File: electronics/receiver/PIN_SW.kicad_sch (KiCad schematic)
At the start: 35 parts, among them J401 Conn_Coaxial, J402 Conn_Coaxial, J403 Conn_Coaxial, J404 Conn_01x06_Male, J405 Conn_01x01_Male, J406 Conn_Coaxial, U401 AS179-92LF, U402 AS179-92LF, U403 AMS1117-5.0, U404 AS179-92LF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

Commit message: Add values
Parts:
- C401, C402, C403, C404, C410, C412: value C -> 1n0
- C405, C406, C407, C408: value C -> 100p
- C409, C411: value C -> 100n
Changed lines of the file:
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@@
       (effects (font (size 1.27 1.27)) (justify left))
     )
-    (property "Value" "C" (id 1) (at 124.46 116.8399 0)
+    (property "Value" "100p" (id 1) (at 124.46 116.8399 0)
       (effects (font (size 1.27 1.27)) (justify left))
     )
@@
       (effects (font (size 1.27 1.27)) (justify left))
     )
-    (property "Value" "C" (id 1) (at 190.5 116.8399 0)
+    (property "Value" "100p" (id 1) (at 190.5 116.8399 0)
       (effects (font (size 1.27 1.27)) (justify left))
     )
@@
     (in_bom yes) (on_board yes) (fields_autoplaced)
     (property "Reference" "C403" (id 0) (at 66.04 147.5445 90))
-    (property "Value" "C" (id 1) (at 66.04 150.3196 90))
+    (property "Value" "1n0" (id 1) (at 66.04 150.3196 90))
     (property "Footprint" "Capacitor_SMD:C_0805_2012Metric" (id 2) (at 69.85 152.7048 0)
       (effects (font (size 1.27 1.27)) hide)
@@
     (in_bom yes) (on_board yes) (fields_autoplaced)
     (property "Reference" "C412" (id 0) (at 218.44 63.9985 90))
-    (property "Value" "C" (id 1) (at 218.44 66.7736 90))
+    (property "Value" "1n0" (id 1) (at 218.44 66.7736 90))
     (property "Footprint" "Capacitor_SMD:C_0805_2012Metric" (id 2) (at 222.25 60.6552 0)
       (effects (font (size 1.27 1.27)) hide)
@@
     (in_bom yes) (on_board yes) (fields_autoplaced)
     (property "Reference" "C404" (id 0) (at 71.12 91.9385 90))
-    (property "Value" "C" (id 1) (at 71.12 94.7136 90))
+    (property "Value" "1n0" (id 1) (at 71.12 94.7136 90))
     (property "Footprint" "Capacitor_SMD:C_0805_2012Metric" (id 2) (at 67.31 88.5952 0)
       (effects (font (size 1.27 1.27)) hide)
@@
       (effects (font (size 1.27 1.27)) (justify left))
     )
-    (property "Value" "C" (id 1) (at 179.07 116.8399 0)
+    (property "Value" "100p" (id 1) (at 179.07 116.8399 0)
       (effects (font (size 1.27 1.27)) (justify left))
     )
@@
   (symbol (lib_id "Device:C") (at 50.8 78.74 270) (unit 1)
     (in_bom yes) (on_board yes) (fields_autoplaced)
-    (property "Reference" "C402" (id 0) (at 50.8 72.6145 90))
-    (property "Value" "C" (id 1) (at 50.8 75.3896 90))
+    (property "Reference" "C402" (id 0) (at 50.8 71.12 90))
+    (property "Value" "1n0" (id 1) (at 50.8 73.66 90))
     (property "Footprint" "Capacitor_SMD:C_0805_2012Metric" (id 2) (at 46.99 79.7052 0)
       (effects (font (size 1.27 1.27)) hide)
@@
       (effects (font (size 1.27 1.27)) (justify left))
     )
-    (property "Value" "C" (id 1) (at 35.941 136.3222 0)
+    (property "Value" "1n0" (id 1) (at 35.941 136.3222 0)
       (effects (font (size 1.27 1.27)) (justify left))
     )
@@
     (in_bom yes) (on_board yes) (fields_autoplaced)
     (property "Reference" "C410" (id 0) (at 207.01 72.6145 90))
-    (property "Value" "C" (id 1) (at 207.01 75.3896 90))
+    (property "Value" "1n0" (id 1) (at 207.01 75.3896 90))
     (property "Footprint" "Capacitor_SMD:C_0805_2012Metric" (id 2) (at 210.82 79.7052 0)
       (effects (font (size 1.27 1.27)) hide)
@@
       (effects (font (size 1.27 1.27)) (justify left))
     )
-    (property "Value" "C" (id 1) (at 213.36 137.1599 0)
+    (property "Value" "100n" (id 1) (at 213.36 137.1599 0)
       (effects (font (size 1.27 1.27)) (justify left))
     )
@@
       (effects (font (size 1.27 1.27)) (justify left))
     )
-    (property "Value" "C" (id 1) (at 134.62 116.8399 0)
+    (property "Value" "100p" (id 1) (at 134.62 116.8399 0)
       (effects (font (size 1.27 1.27)) (justify left))
     )
@@
       (effects (font (size 1.27 1.27)) (justify left))
     )
-    (property "Value" "C" (id 1) (at 195.58 151.1299 0)
-      (effects (font (size 1.27 1.27)) (justify left))
-    )
+    (property "Value" "100n" (id 1) (at 195.58 151.1299 0)
+      (effects (font (size 1.27 1.27)) (justify left))
+    )

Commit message: Update values
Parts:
- R401, R402, R404, R405: value R -> 68R
- R403, R406, R408, R410: value R -> NF
- R407, R409, R411: value R -> 0R
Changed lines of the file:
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@@
+    (effects (font (size 1.27 1.27)) (justify left bottom))
+  )
+  (label "Loss = 16 dB" (at 78.74 143.51 0)
     (effects (font (size 1.27 1.27)) (justify left bottom))
   )
@@
   (symbol (lib_id "Device:R") (at 226.06 146.05 0) (unit 1)
     (in_bom yes) (on_board yes) (fields_autoplaced)
-    (property "Reference" "R411" (id 0) (at 227.838 145.2153 0)
-      (effects (font (size 1.27 1.27)) (justify left))
-    )
-    (property "Value" "R" (id 1) (at 227.838 147.7522 0)
+    (property "Reference" "R411" (id 0) (at 228.6 144.7799 0)
+      (effects (font (size 1.27 1.27)) (justify left))
+    )
+    (property "Value" "0R" (id 1) (at 228.6 147.3199 0)
       (effects (font (size 1.27 1.27)) (justify left))
     )
@@
   (symbol (lib_id "Device:R") (at 220.98 129.54 0) (unit 1)
     (in_bom yes) (on_board yes) (fields_autoplaced)
-    (property "Reference" "R408" (id 0) (at 222.758 128.7053 0)
-      (effects (font (size 1.27 1.27)) (justify left))
-    )
-    (property "Value" "R" (id 1) (at 222.758 131.2422 0)
+    (property "Reference" "R408" (id 0) (at 223.52 128.2699 0)
+      (effects (font (size 1.27 1.27)) (justify left))
+    )
+    (property "Value" "NF" (id 1) (at 223.52 130.8099 0)
       (effects (font (size 1.27 1.27)) (justify left))
     )
@@
   (symbol (lib_id "Device:R") (at 226.06 129.54 0) (unit 1)
     (in_bom yes) (on_board yes) (fields_autoplaced)
-    (property "Reference" "R410" (id 0) (at 227.838 128.7053 0)
-      (effects (font (size 1.27 1.27)) (justify left))
-    )
-    (property "Value" "R" (id 1) (at 227.838 131.2422 0)
+    (property "Reference" "R410" (id 0) (at 228.6 128.2699 0)
+      (effects (font (size 1.27 1.27)) (justify left))
+    )
+    (property "Value" "NF" (id 1) (at 228.6 130.8099 0)
       (effects (font (size 1.27 1.27)) (justify left))
     )
@@
   (symbol (lib_id "Device:R") (at 214.63 129.54 0) (unit 1)
     (in_bom yes) (on_board yes) (fields_autoplaced)
-    (property "Reference" "R406" (id 0) (at 216.408 128.7053 0)
-      (effects (font (size 1.27 1.27)) (justify left))
-    )
-    (property "Value" "R" (id 1) (at 216.408 131.2422 0)
+    (property "Reference" "R406" (id 0) (at 217.17 128.2699 0)
+      (effects (font (size 1.27 1.27)) (justify left))
+    )
+    (property "Value" "NF" (id 1) (at 217.17 130.8099 0)
       (effects (font (size 1.27 1.27)) (justify left))
     )
@@
   (symbol (lib_id "Device:R") (at 74.93 158.75 0) (unit 1)
     (in_bom yes) (on_board yes) (fields_autoplaced)
-    (property "Reference" "R401" (id 0) (at 76.708 157.8415 0)
-      (effects (font (size 1.27 1.27)) (justify left))
-    )
-    (property "Value" "R" (id 1) (at 76.708 160.6166 0)
+    (property "Reference" "R401" (id 0) (at 77.47 157.4799 0)
+      (effects (font (size 1.27 1.27)) (justify left))
+    )
+    (property "Value" "68R" (id 1) (at 77.47 160.0199 0)
       (effects (font (size 1.27 1.27)) (justify left))
     )
@@
   (symbol (lib_id "Device:R") (at 90.17 153.67 270) (unit 1)
     (in_bom yes) (on_board yes) (fields_autoplaced)
-    (property "Reference" "R404" (id 0) (at 90.17 148.6875 90))
-    (property "Value" "R" (id 1) (at 90.17 151.4626 90))
+    (property "Reference" "R404" (id 0) (at 90.17 147.32 90))
+    (property "Value" "68R" (id 1) (at 90.17 149.86 90))
     (property "Footprint" "Resistor_SMD:R_0805_2012Metric_Pad1.20x1.40mm_HandSolder" (id 2) (at 90.17 151.892 90)
       (effects (font (size 1.27 1.27)) hide)
@@
   (symbol (lib_id "Device:R") (at 95.25 158.75 0) (unit 1)
     (in_bom yes) (on_board yes) (fields_autoplaced)
-    (property "Reference" "R405" (id 0) (at 97.028 157.8415 0)
-      (effects (font (size 1.27 1.27)) (justify left))
-    )
-    (property "Value" "R" (id 1) (at 97.028 160.6166 0)
+    (property "Reference" "R405" (id 0) (at 97.79 157.4799 0)
+      (effects (font (size 1.27 1.27)) (justify left))
+    )
+    (property "Value" "68R" (id 1) (at 97.79 160.0199 0)
       (effects (font (size 1.27 1.27)) (justify left))
     )
@@
   (symbol (lib_id "Device:R") (at 80.01 153.67 270) (unit 1)
     (in_bom yes) (on_board yes) (fields_autoplaced)
-    (property "Reference" "R402" (id 0) (at 80.01 148.6875 90))
-    (property "Value" "R" (id 1) (at 80.01 151.4626 90))
+    (property "Reference" "R402" (id 0) (at 80.01 147.32 90))
+    (property "Value" "68R" (id 1) (at 80.01 149.86 90))
     (property "Footprint" "Resistor_SMD:R_0805_2012Metric_Pad1.20x1.40mm_HandSolder" (id 2) (at 80.01 151.892 90)
       (effects (font (size 1.27 1.27)) hide)
@@
   (symbol (lib_id "Device:R") (at 85.09 158.75 0) (unit 1)
     (in_bom yes) (on_board yes) (fields_autoplaced)
-    (property "Reference" "R403" (id 0) (at 86.868 157.8415 0)
-      (effects (font (size 1.27 1.27)) (justify left))
-    )
-    (property "Value" "R" (id 1) (at 86.868 160.6166 0)
+    (property "Reference" "R403" (id 0) (at 87.63 157.4799 0)
+      (effects (font (size 1.27 1.27)) (justify left))
+    )
+    (property "Value" "NF" (id 1) (at 87.63 160.0199 0)
       (effects (font (size 1.27 1.27)) (justify left))
     )
@@
   (symbol (lib_id "Device:R") (at 214.63 146.05 0) (unit 1)
     (in_bom yes) (on_board yes) (fields_autoplaced)
-    (property "Reference" "R407" (id 0) (at 216.408 145.2153 0)
-      (effects (font (size 1.27 1.27)) (justify left))
-    )
-    (property "Value" "R" (id 1) (at 216.408 147.7522 0)
+    (property "Reference" "R407" (id 0) (at 217.17 144.7799 0)
+      (effects (font (size 1.27 1.27)) (justify left))
+    )
+    (property "Value" "0R" (id 1) (at 217.17 147.3199 0)
       (effects (font (size 1.27 1.27)) (justify left))
     )
@@
   (symbol (lib_id "Device:R") (at 220.98 146.05 0) (unit 1)
     (in_bom yes) (on_board yes) (fields_autoplaced)
-    (property "Reference" "R409" (id 0) (at 222.758 145.2153 0)
-      (effects (font (size 1.27 1.27)) (justify left))
-    )
-    (property "Value" "R" (id 1) (at 222.758 147.7522 0)
-      (effects (font (size 1.27 1.27)) (justify left))
-    )
+    (property "Reference" "R409" (id 0) (at 223.52 144.7799 0)
+      (effects (font (size 1.27 1.27)) (justify left))
+    )
+    (property "Value" "0R" (id 1) (at 223.52 147.3199 0)
+      (effects (font (size 1.27 1.27)) (justify left))
+    )

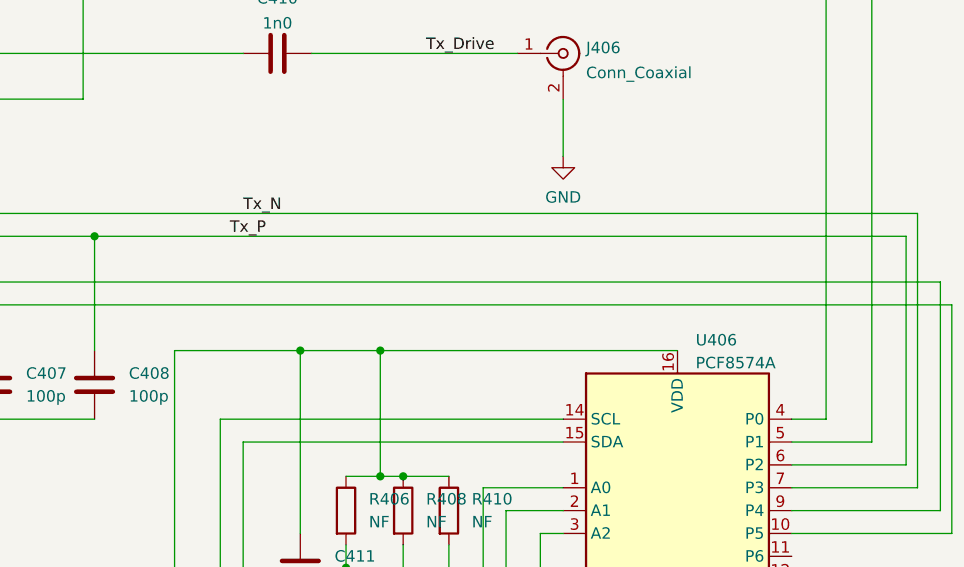
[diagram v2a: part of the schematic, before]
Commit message: Control definition
Various updates and new Software interface description
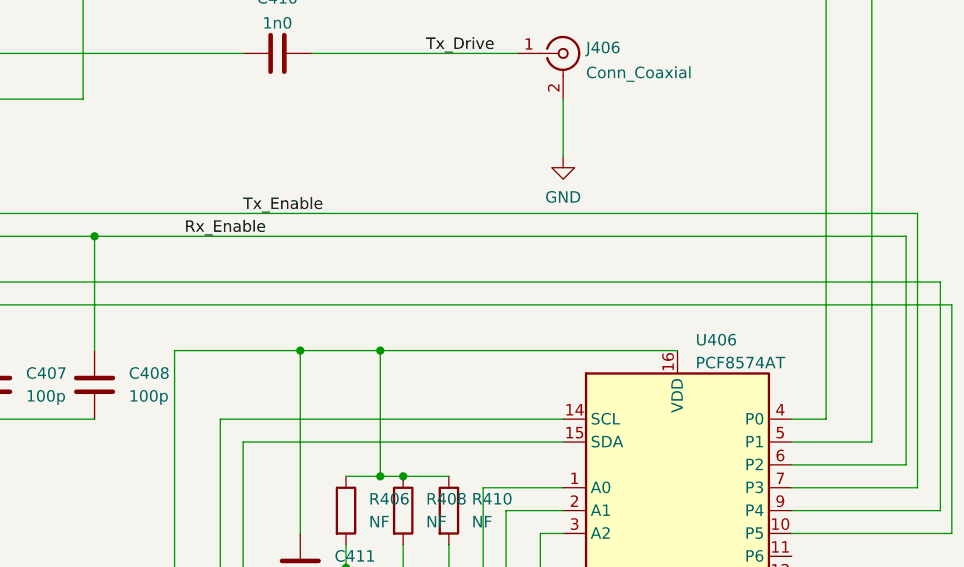
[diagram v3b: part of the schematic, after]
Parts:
- U406: value PCF8574A -> PCF8574AT
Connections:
- net Tx_N is gone; now on net Tx_Enable: C407.1, U404.6 (V2), U406.7 (P3)
- net Tx_P is gone; now on net Rx_Enable: C408.1, U404.4 (V1), U406.6 (P2)
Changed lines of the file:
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@@
     (effects (font (size 1.27 1.27)) (justify left bottom))
   )
-  (label "Tx_N" (at 203.2 96.52 0)
+  (label "Tx_Enable" (at 203.2 96.52 0)
     (effects (font (size 1.27 1.27)) (justify left bottom))
   )
-  (label "Tx_P" (at 205.74 99.06 180)
+  (label "Rx_Enable" (at 205.74 99.06 180)
     (effects (font (size 1.27 1.27)) (justify right bottom))
   )
@@
       (effects (font (size 1.27 1.27)) (justify left))
     )
-    (property "Value" "PCF8574A" (id 1) (at 253.4794 113.1371 0)
-      (effects (font (size 1.27 1.27)) (justify left))
-    )
+    (property "Value" "PCF8574AT" (id 1) (at 253.4794 113.1371 0)
+      (effects (font (size 1.27 1.27)) (justify left))
+    )

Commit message: Repair
Fix Github commit problem
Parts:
- added C407: 4.7uF 16V, symbol Device:C_Polarized
- added C408, C411: 4.7uF 10V, symbol Device:C_Polarized
- renumbered C407 to C409, C408 to C410, C409 to C412, C410 to C413, C411 to C414, C412 to C415
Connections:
- net +12V: now also C407.1
- net +3.3V: now also C411.1
- net +5V: now also C408.1
- net GND: now also C407.2, C408.2, C411.2
